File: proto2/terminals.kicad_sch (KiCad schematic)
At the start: 111 parts, among them J1 Output 1, J10 Output, J11 Device, J2 Main Power, J3 Output, J4 Output, J5 Device, J6 Output, J7 Device, J8 Output, J9 Device

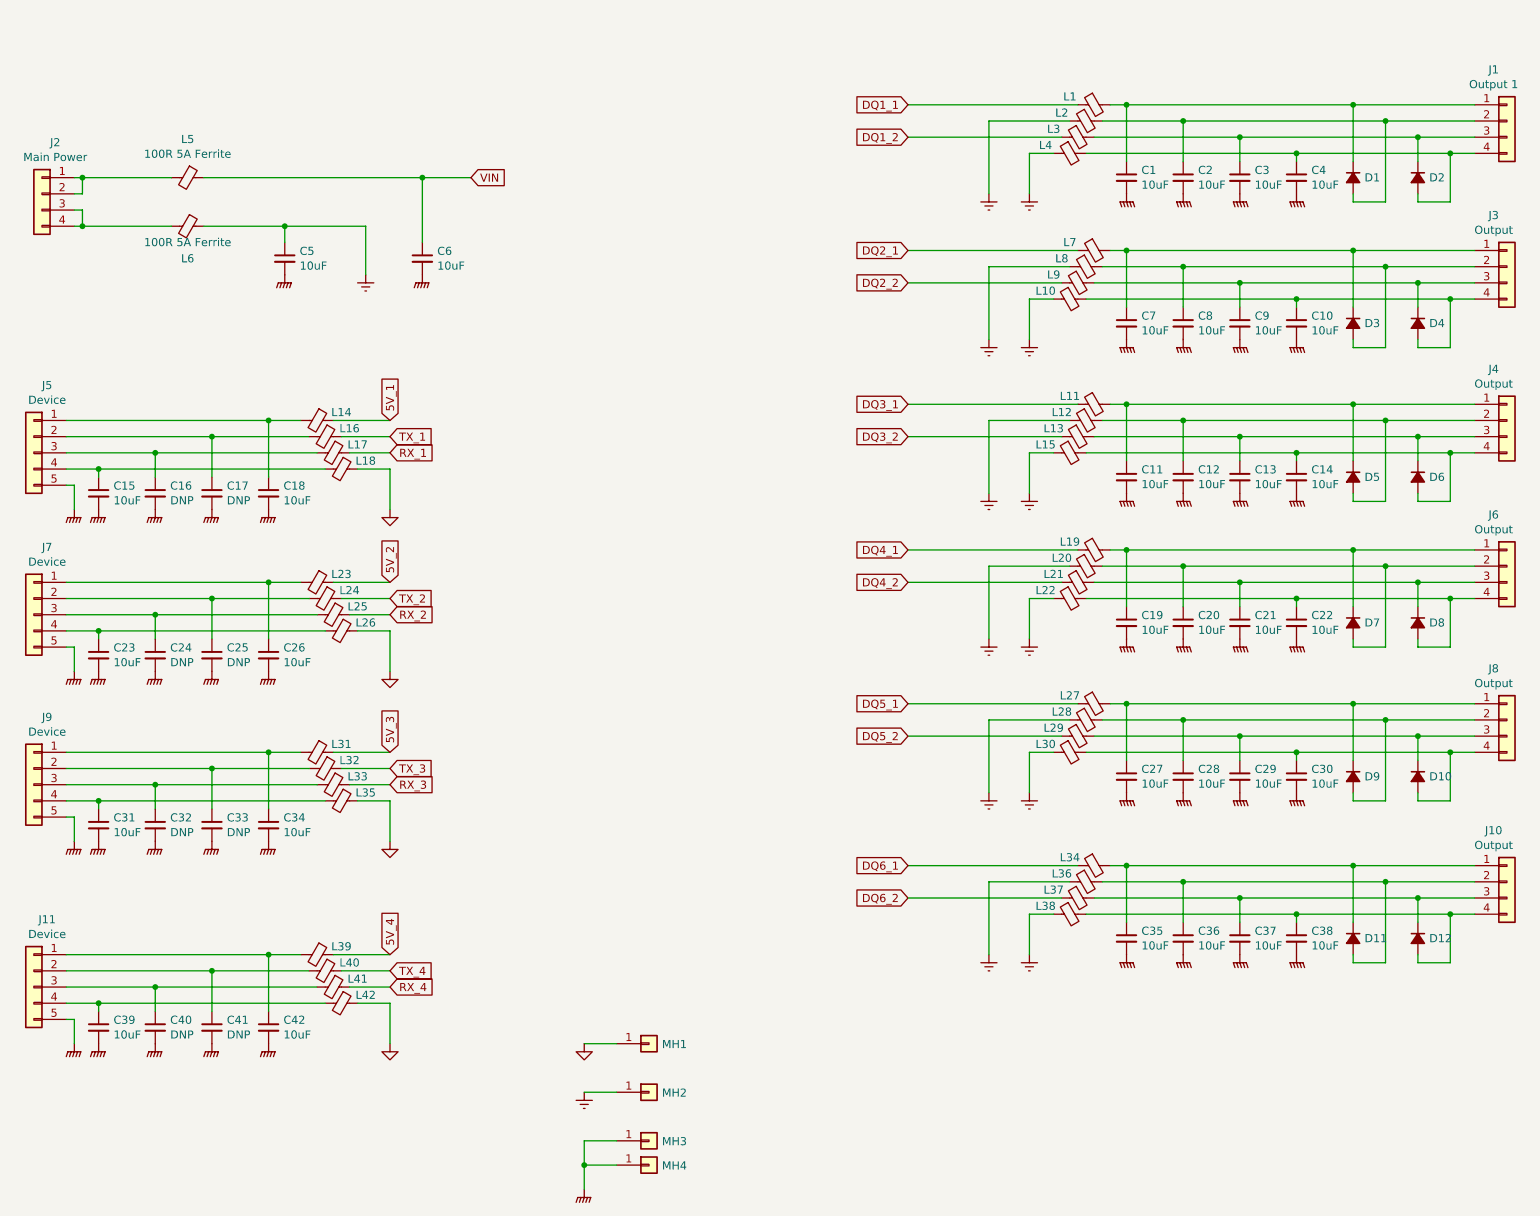
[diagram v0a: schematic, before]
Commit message: Added another 2 outputs and re-routed board.
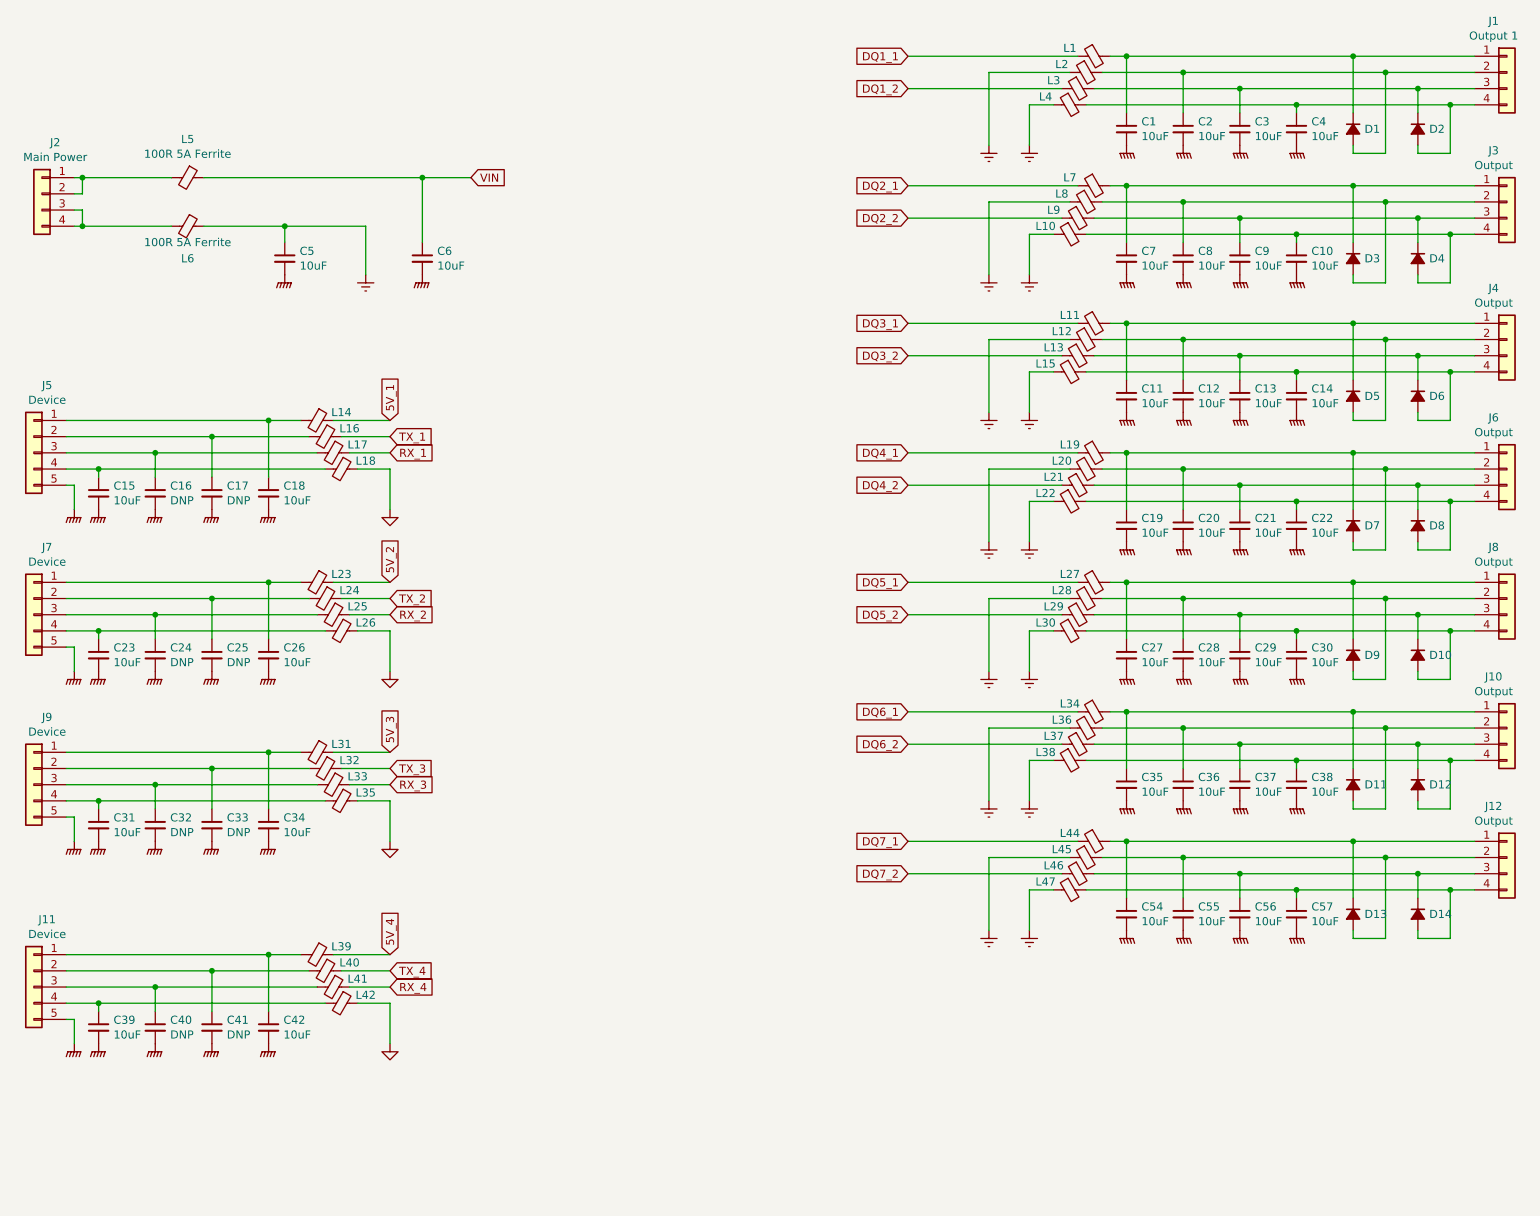
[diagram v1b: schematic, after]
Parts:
- removed MH1, MH2, MH3, MH4: Conn_01x01, STD-xxx:STD-.125_wide, symbol Connector_Generic:Conn_01x01
- added C54, C55, C56, C57: 10uF, Capacitor_SMD:C_0805_2012Metric, symbol Device:C_Small
- added D13, D14: D_Small_ALT, Diode_SMD:D_SOD-123F, symbol Device:D_Small_ALT
- added J12: Output, Connector_BCR:Phoenix_Contact_PST_4, symbol Connector_Generic:Conn_01x04
- added L44, L45, L46, L47: 1A Ferrite, Resistor_SMD:R_1206_3216Metric, symbol Device:Ferrite_Bead_Small
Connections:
- net Earth: now also L45.1, L47.1
- net GNDPWR: now also C54.2, C55.2, C56.2, C57.2
- new net: C57.1, D14.2 (A), J12.4 (Pin_4), L47.2
- new net: C56.1, D14.1 (K), J12.3 (Pin_3), L46.2
- new net: C54.1, D13.1 (K), J12.1 (Pin_1), L44.2
- new net: C55.1, D13.2 (A), J12.2 (Pin_2), L45.2
- new net DQ7_1: L44.1
- new net DQ7_2: L46.1
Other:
- title: (none) -> Greenhouse 2.0 IO Board
- moved on the sheet: C1, C10, C11, C12, C13, C14, C19, C2, C20, C21, C22, C27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

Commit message: Working in suggestions from CFL review.
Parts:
- removed C16, C17, C24, C25, C32, C33, C40, C41: DNP, Capacitor_SMD:C_0805_2012Metric, symbol Device:C_Small
- removed L16, L17, L24, L25, L32, L33, L40, L41: 0R, Resistor_SMD:R_0805_2012Metric, symbol Device:Ferrite_Bead_Small
- added C? (x38): 10uF, Capacitor_SMD:C_0805_2012Metric, symbol Device:C_Small
- added R? (x36): Rcrit, symbol Device:R_Small
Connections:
- net 5V_1: now also R?.1
- net 5V_2: now also R?.1
- net 5V_3: now also R?.1
- net 5V_4: now also R?.1
- net DQ1_1: now also R?.1
- net DQ1_2: now also R?.1
- net DQ2_1: now also R?.1
- net DQ2_2: now also R?.1
- net DQ3_1: now also R?.1
- net DQ3_2: now also R?.1
- net DQ4_1: now also R?.1
- net DQ4_2: now also R?.1
- net DQ5_1: now also R?.1
- net DQ5_2: now also R?.1
- net DQ6_1: now also R?.1
- net DQ6_2: now also R?.1
- net DQ7_1: now also R?.1
- net DQ7_2: now also R?.1
- net Earth: now also R?.1, R?.1, R?.1, R?.1, R?.1, R?.1, R?.1, R?.1, R?.1, R?.1, R?.1, R?.1, R?.1, R?.1
- net GNDPWR: now also C?.2, C?.2, C?.2, C?.2, C?.2, C?.2, C?.2, C?.2, C?.2, C?.2, C?.2, C?.2, C?.2, C?.2, C?.2, C?.2, C?.2, C?.2, C?.2, C?.2, C?.2, C?.2, C?.2, C?.2, C?.2, C?.2, C?.2, C?.2, C?.2, C?.2, C?.2, C?.2, C?.2, C?.2, C?.2, C?.2, C?.2, C?.2
- net RX_1: now also J5.3 (Pin_3)
- net RX_2: now also J7.3 (Pin_3)
- net RX_3: now also J9.3 (Pin_3)
- net RX_4: now also J11.3 (Pin_3)
- net TX_1: now also J5.2 (Pin_2)
- net TX_2: now also J7.2 (Pin_2)
- net TX_3: now also J9.2 (Pin_2)
- net TX_4: now also J11.2 (Pin_2)
- net at J2.1 (Pin_1), J2.2 (Pin_2), L5.2: now also C?.1
- net at J2.3 (Pin_3), J2.4 (Pin_4), L6.2: now also C?.1
- removed net GND: L18.1, L26.1, L35.1, L42.1
- new net: C?.1, R?.2 (x36)
- new net GND_1: L18.1, R?.1
- new net GND_2: L26.1, R?.1
- new net GND_3: L35.1, R?.1
- new net GND_4: L42.1, R?.1
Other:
- moved on the sheet: C1, C10, C11, C12, C13, C14, C15, C18, C19, C2, C20, C21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

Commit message: Changes suggested by CFL.
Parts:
- added R100, R107, R108, R109, R110, R111, R112, R119, R120, R121, R122, R123, R124, R129, R130, R131, R132, R61, R62, R63, R64, R69, R70, R71, R72, R73, R74, R75, R76, R83, R84, R85, R86, R87, R88, R95, R96, R97, R98, R99: 0R, Resistor_SMD:R_0805_2012Metric, symbol Device:R_Small
- J1, J10, J2, J3, J4, J6, J8: footprint BCR_Connector:Phoenix_Contact_PST_4 -> Connector_BCR:Phoenix_Contact_PST_4
- J11, J5, J7, J9: footprint BCR_Connector:Phoenix_Contact_PST_5 -> Connector_BCR:Phoenix_Contact_PST_5
- L1, L10, L11, L12, L13, L15, L19, L2, L20, L21, L22, L27, L28, L29, L3, L30, L34, L36, L37, L38, L4, L44, L45, L46, L47, L7, L8, L9: value 1A Ferrite -> 10uH 900mA; footprint Resistor_SMD:R_1206_3216Metric -> Inductor_SMD:L_1210_3225Metric; LCSC C405012 -> C90321; Manufacturer (none) -> Taiyo Yuden; Part Number (none) -> CBC3225T100KR
- L14, L18, L23, L26, L31, L35, L39, L42: value 500mA Ferrite -> 4.7uH 800mA; LCSC C1017 -> C86090; Manufacturer (none) -> Murata; Part Number (none) -> LQM21PN4R7MGRD
- R101, R102, R103, R104, R105, R106, R113, R114, R115, R116, R117, R118, R125, R126, R127, R128, R133, R134, R135, R136, R65, R66, R67, R68, R77, R78, R79, R80, R81, R82, R89, R90, R91, R92, R93, R94: renamed from R?; value Rcrit -> 0R; footprint (none) -> Resistor_SMD:R_0805_2012Metric; LCSC (none) -> C17477
- gave numbers to parts that had none: 38
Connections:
- net Earth: now also R69.1; no longer C5.1
- net VIN: now also R72.1; no longer C6.1
- net at D1.1 (K), J1.1 (Pin_1), L1.2: now also R64.1; no longer C1.1
- net at D1.2 (A), J1.2 (Pin_2), L2.2: now also R63.1; no longer C2.1
- net at D2.1 (K), J1.3 (Pin_3), L3.2: now also R62.1; no longer C3.1
- net at D2.2 (A), J1.4 (Pin_4), L4.2: now also R61.1; no longer C4.1
- net at J2.1 (Pin_1), J2.2 (Pin_2), L5.2: now also R70.1; no longer C32.1
- net at J2.3 (Pin_3), J2.4 (Pin_4), L6.2: now also R71.1; no longer C33.1
- net at J11.1 (Pin_1), L39.2: now also R119.1; no longer C42.1
- net at J11.4 (Pin_4), L42.2: now also R120.1; no longer C39.1
- net at D3.1 (K), J3.1 (Pin_1), L7.2: now also R76.1; no longer C7.1
- net at D3.2 (A), J3.2 (Pin_2), L8.2: now also R75.1; no longer C8.1
- net at D4.1 (K), J3.3 (Pin_3), L9.2: now also R74.1; no longer C9.1
- net at D4.2 (A), J3.4 (Pin_4), L10.2: now also R73.1; no longer C10.1
- net at D5.1 (K), J4.1 (Pin_1), L11.2: now also R88.1; no longer C11.1
- net at D5.2 (A), J4.2 (Pin_2), L12.2: now also R87.1; no longer C12.1
- net at D6.1 (K), J4.3 (Pin_3), L13.2: now also R86.1; no longer C13.1
- net at D6.2 (A), J4.4 (Pin_4), L15.2: now also R85.1; no longer C14.1
- net at D7.1 (K), J6.1 (Pin_1), L19.2: now also R100.1; no longer C19.1
- net at D7.2 (A), J6.2 (Pin_2), L20.2: now also R99.1; no longer C20.1
- net at D8.1 (K), J6.3 (Pin_3), L21.2: now also R98.1; no longer C21.1
- net at D8.2 (A), J6.4 (Pin_4), L22.2: now also R97.1; no longer C22.1
- net at D9.1 (K), J8.1 (Pin_1), L27.2: now also R112.1; no longer C27.1
- net at D9.2 (A), J8.2 (Pin_2), L28.2: now also R111.1; no longer C28.1
- net at D10.1 (K), J8.3 (Pin_3), L29.2: now also R110.1; no longer C29.1
- net at D10.2 (A), J8.4 (Pin_4), L30.2: now also R109.1; no longer C30.1
- net at D11.1 (K), J10.1 (Pin_1), L34.2: now also R124.1; no longer C35.1
- net at D11.2 (A), J10.2 (Pin_2), L36.2: now also R123.1; no longer C36.1
- net at D12.1 (K), J10.3 (Pin_3), L37.2: now also R122.1; no longer C37.1
- net at D12.2 (A), J10.4 (Pin_4), L38.2: now also R121.1; no longer C38.1
- net at J9.4 (Pin_4), L35.2: now also R108.1; no longer C31.1
- net at J7.1 (Pin_1), L23.2: now also R95.1; no longer C26.1
- net at J7.4 (Pin_4), L26.2: now also R96.1; no longer C23.1
- net at J5.4 (Pin_4), L18.2: now also R84.1; no longer C15.1
- net at J5.1 (Pin_1), L14.2: now also R83.1; no longer C18.1
- net at J9.1 (Pin_1), L31.2: now also R107.1; no longer C34.1
- net at D14.2 (A), J12.4 (Pin_4), L47.2: now also R129.1; no longer C57.1
- net at D14.1 (K), J12.3 (Pin_3), L46.2: now also R130.1; no longer C56.1
- net at D13.1 (K), J12.1 (Pin_1), L44.2: now also R132.1; no longer C54.1
- net at D13.2 (A), J12.2 (Pin_2), L45.2: now also R131.1; no longer C55.1
- new net: C6.1, R72.2
- new net: C5.1, R69.2
- new net: C31.1, R108.2
- new net: C39.1, R120.2
- new net: C42.1, R119.2
- new net: C26.1, R95.2
- new net: C23.1, R96.2
- new net: C15.1, R84.2
- new net: C18.1, R83.2
- new net: C35.1, R124.2
- new net: C36.1, R123.2
- new net: C37.1, R122.2
- new net: C38.1, R121.2
- new net: C30.1, R109.2
- new net: C29.1, R110.2
- new net: C28.1, R111.2
- new net: C27.1, R112.2
- new net: C19.1, R100.2
- new net: C20.1, R99.2
- new net: C21.1, R98.2
- new net: C22.1, R97.2
- new net: C14.1, R85.2
- new net: C13.1, R86.2
- new net: C12.1, R87.2
- new net: C11.1, R88.2
- new net: C7.1, R76.2
- new net: C8.1, R75.2
- new net: C9.1, R74.2
- new net: C10.1, R73.2
- new net: C4.1, R61.2
- new net: C3.1, R62.2
- new net: C2.1, R63.2
- new net: C1.1, R64.2
- new net: C34.1, R107.2
- new net: C57.1, R129.2
- new net: C54.1, R132.2
- new net: C32.1, R70.2
- new net: C55.1, R131.2
- new net: C56.1, R130.2
- new net: C33.1, R71.2
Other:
- moved on the sheet: C15, C18, C19, C20, C21, C22, C23, C26, C31, C32, C33, C34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
